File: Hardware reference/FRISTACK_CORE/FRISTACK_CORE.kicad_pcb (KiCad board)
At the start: 2 copper layers, 51 x 51 mm, 78 parts, among them J1 USB_C_Receptacle_USB2.0_16P, J2 JTAG_PIN_HEADER, J4 Conn_01x13_Socket, J5 Conn_01x13_Socket, J6 Conn_01x02_Pin, J7 Conn_01x02_Pin, U1 TPS62840DLCR, U2 USBLC6-2SC6, U3 ESP32-S3-MINI-1U, U4 FSUSB42MUX, U5 SN65HVD232, Y1 32.768 kHz

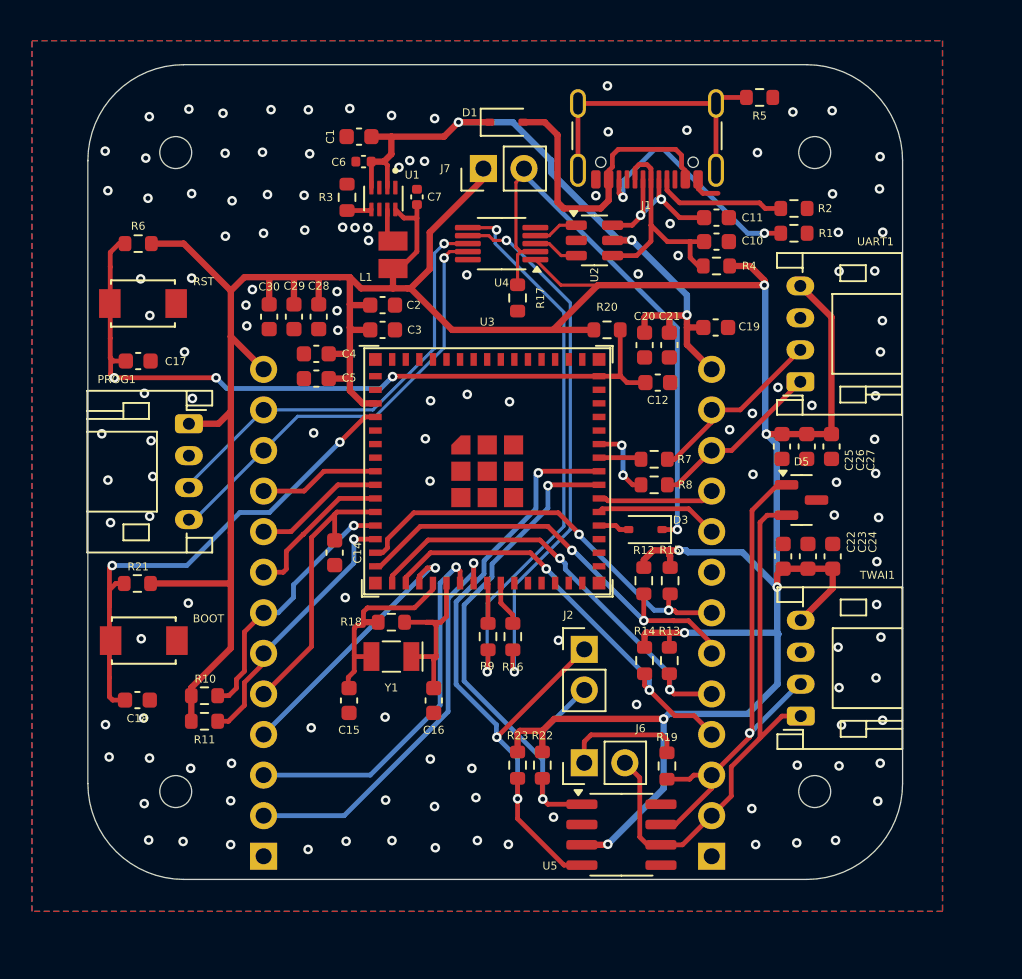
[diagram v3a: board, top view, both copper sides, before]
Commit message: Reworked CORE and adjusted header pins
Added USB switch and MCP73871 for charging battery and powering the system. Changed GPIO14 to BAT, dedicated for battery.
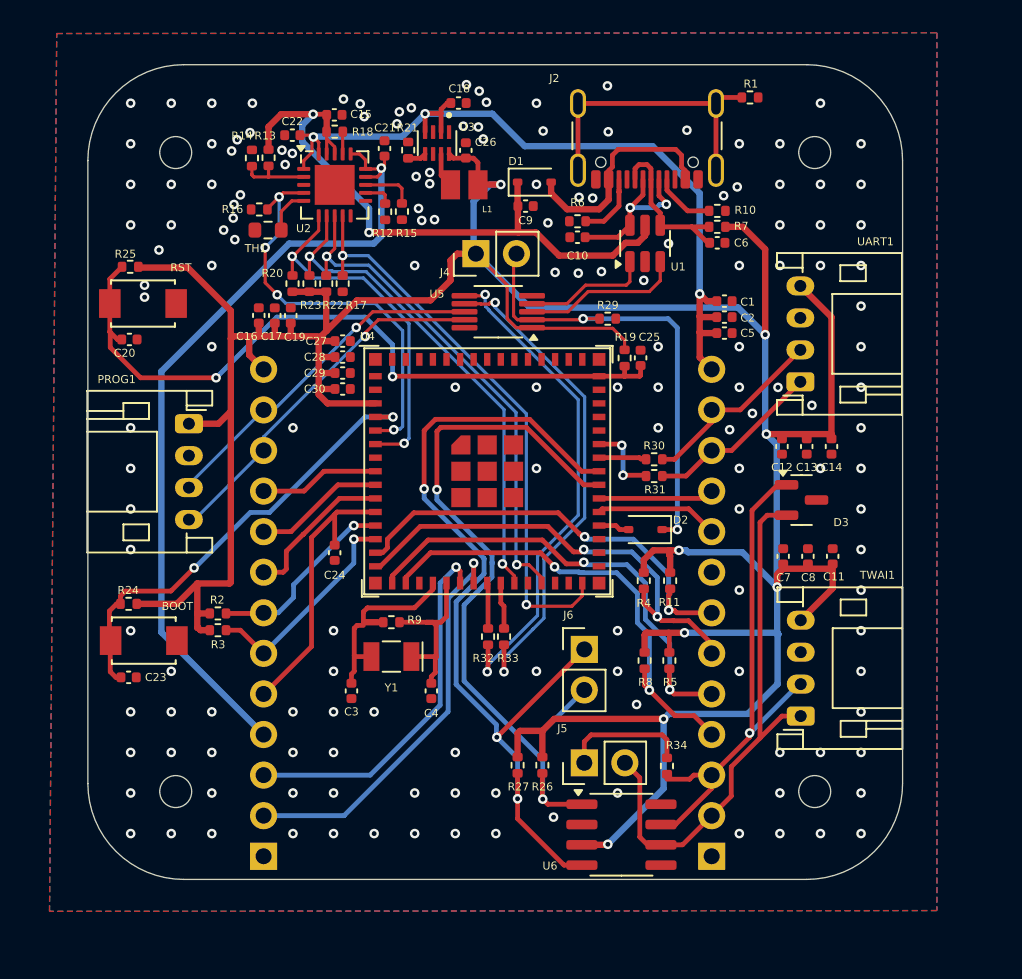
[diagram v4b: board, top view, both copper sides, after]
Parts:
- removed the C1 at (144.0, 76.5)
- removed the C11 at (166.3, 81.6)
- removed the C7 at (147.6, 80.3)
- removed J7: Conn_01x02_Pin, Connector_PinHeader_2.54mm:PinHeader_1x02_P2.54mm_Vertical
- removed the R1 at (171.2, 82.5)
- removed the R2 at (171.2, 81.0)
- removed the R3 at (143.2, 80.3)
- removed the R4 at (166.3, 84.6)
- removed the U4 at (152.9, 83.2)
- added C15: 10uf, Capacitor_SMD:C_0402_1005Metric, F.Cu at (142.4, 75.1)
- added C18: 4.7uF, Capacitor_SMD:C_0402_1005Metric, F.Cu at (150.2, 74.4)
- added C21: 4.7uF, Capacitor_SMD:C_0402_1005Metric, F.Cu at (145.6, 77.2)
- added C22: 4.7uF, Capacitor_SMD:C_0402_1005Metric, F.Cu at (139.8, 76.4)
- added C26: 10uF, Capacitor_SMD:C_0402_1005Metric, F.Cu at (150.7, 77.4)
- added C9: 10uf, Capacitor_SMD:C_0402_1005Metric, F.Cu at (154.4, 80.8)
- added J4: Conn_01x02_Pin, Connector_PinHeader_2.54mm:PinHeader_1x02_P2.54mm_Vertical, F.Cu at (151.3, 83.8)
- added R10: 5.1K, Resistor_SMD:R_0402_1005Metric, F.Cu at (166.4, 81.2)
- added R12: 20k, Resistor_SMD:R_0402_1005Metric, F.Cu at (145.6, 81.2)
- added R13: 330k, Resistor_SMD:R_0402_1005Metric, F.Cu at (138.3, 77.8)
- added R14: 110k, Resistor_SMD:R_0402_1005Metric, F.Cu at (137.3, 77.8)
- added R15: 2k, Resistor_SMD:R_0402_1005Metric, F.Cu at (146.7, 81.2)
- added R16: 10k, Resistor_SMD:R_0402_1005Metric, F.Cu at (137.7, 81.1)
- added R18: 10k, Resistor_SMD:R_0402_1005Metric, F.Cu at (142.4, 76.2)
- added R20: 10k, Resistor_SMD:R_0402_1005Metric, F.Cu at (139.8, 85.7)
- added R21: 267k, Resistor_SMD:R_0402_1005Metric, F.Cu at (147.1, 77.3)
- added R22: 10k, Resistor_SMD:R_0402_1005Metric, F.Cu at (141.9, 85.7)
- added R23: 10k, Resistor_SMD:R_0402_1005Metric, F.Cu at (140.9, 85.7)
- added R29: 10K, Resistor_SMD:R_0402_1005Metric, F.Cu at (159.5, 87.9)
- added R6: 5.1K, Resistor_SMD:R_0402_1005Metric, F.Cu at (157.7, 81.8)
- added R7: 10K, Resistor_SMD:R_0402_1005Metric, F.Cu at (166.4, 82.2)
- added TH1: 10k, Resistor_SMD:R_0603_1608Metric, F.Cu at (138.3, 82.4)
- added U1: USBLC6-2SC6, Package_TO_SOT_SMD:SOT-23-6, F.Cu at (161.9, 83.2)
- added U5: FSUSB42MUX, Package_SO:MSOP-10_3x3mm_P0.5mm, F.Cu at (152.7, 87.5)
- C1: renamed from C19; footprint Capacitor_SMD:C_0603_1608Metric -> Capacitor_SMD:C_0402_1005Metric
- C10: footprint Capacitor_SMD:C_0603_1608Metric -> Capacitor_SMD:C_0402_1005Metric
- C11: renamed from C24; footprint Capacitor_SMD:C_0603_1608Metric -> Capacitor_SMD:C_0402_1005Metric
- C12: renamed from C25; footprint Capacitor_SMD:C_0603_1608Metric -> Capacitor_SMD:C_0402_1005Metric
- C13: renamed from C26; footprint Capacitor_SMD:C_0603_1608Metric -> Capacitor_SMD:C_0402_1005Metric
- C14: renamed from C27; footprint Capacitor_SMD:C_0603_1608Metric -> Capacitor_SMD:C_0402_1005Metric
- C16: renamed from C28; footprint Capacitor_SMD:C_0603_1608Metric -> Capacitor_SMD:C_0402_1005Metric
- C17: renamed from C29; footprint Capacitor_SMD:C_0603_1608Metric -> Capacitor_SMD:C_0402_1005Metric
- C19: renamed from C30; footprint Capacitor_SMD:C_0603_1608Metric -> Capacitor_SMD:C_0402_1005Metric
- C2: renamed from C20; footprint Capacitor_SMD:C_0603_1608Metric -> Capacitor_SMD:C_0402_1005Metric
- C20: renamed from C17; footprint Capacitor_SMD:C_0603_1608Metric -> Capacitor_SMD:C_0402_1005Metric
- C23: renamed from C18; footprint Capacitor_SMD:C_0603_1608Metric -> Capacitor_SMD:C_0402_1005Metric
- C24: renamed from C14; footprint Capacitor_SMD:C_0603_1608Metric -> Capacitor_SMD:C_0402_1005Metric
- C25: renamed from C12; footprint Capacitor_SMD:C_0603_1608Metric -> Capacitor_SMD:C_0402_1005Metric
- C27: renamed from C2; footprint Capacitor_SMD:C_0603_1608Metric -> Capacitor_SMD:C_0402_1005Metric
- C28: renamed from C3; footprint Capacitor_SMD:C_0603_1608Metric -> Capacitor_SMD:C_0402_1005Metric
- C29: renamed from C4; footprint Capacitor_SMD:C_0603_1608Metric -> Capacitor_SMD:C_0402_1005Metric
- C3: renamed from C15; footprint Capacitor_SMD:C_0603_1608Metric -> Capacitor_SMD:C_0402_1005Metric
- C30: renamed from C5; footprint Capacitor_SMD:C_0603_1608Metric -> Capacitor_SMD:C_0402_1005Metric
- C4: renamed from C16; footprint Capacitor_SMD:C_0603_1608Metric -> Capacitor_SMD:C_0402_1005Metric
- C5: renamed from C21; footprint Capacitor_SMD:C_0603_1608Metric -> Capacitor_SMD:C_0402_1005Metric
- C6: value 4.7uF -> 10uf
- C7: renamed from C22; footprint Capacitor_SMD:C_0603_1608Metric -> Capacitor_SMD:C_0402_1005Metric
- C8: renamed from C23; footprint Capacitor_SMD:C_0603_1608Metric -> Capacitor_SMD:C_0402_1005Metric
- L1: footprint User imports:INDC2016X120N -> User_imports:INDC2016X120N
- R1: renamed from R5; footprint Resistor_SMD:R_0603_1608Metric -> Resistor_SMD:R_0402_1005Metric
- R11: renamed from R15; footprint Resistor_SMD:R_0603_1608Metric -> Resistor_SMD:R_0402_1005Metric
- R17: value 10K -> 10k; footprint Resistor_SMD:R_0603_1608Metric -> Resistor_SMD:R_0402_1005Metric
- R19: renamed from R20; footprint Resistor_SMD:R_0603_1608Metric -> Resistor_SMD:R_0402_1005Metric
- R2: renamed from R10; footprint Resistor_SMD:R_0603_1608Metric -> Resistor_SMD:R_0402_1005Metric
- R24: renamed from R21; footprint Resistor_SMD:R_0603_1608Metric -> Resistor_SMD:R_0402_1005Metric
- R25: renamed from R6; footprint Resistor_SMD:R_0603_1608Metric -> Resistor_SMD:R_0402_1005Metric
- R26: renamed from R22; footprint Resistor_SMD:R_0603_1608Metric -> Resistor_SMD:R_0402_1005Metric
- R27: renamed from R23; footprint Resistor_SMD:R_0603_1608Metric -> Resistor_SMD:R_0402_1005Metric
- R3: renamed from R11; footprint Resistor_SMD:R_0603_1608Metric -> Resistor_SMD:R_0402_1005Metric
- R30: renamed from R7; footprint Resistor_SMD:R_0603_1608Metric -> Resistor_SMD:R_0402_1005Metric
- R31: renamed from R8; footprint Resistor_SMD:R_0603_1608Metric -> Resistor_SMD:R_0402_1005Metric
- R32: renamed from R9; footprint Resistor_SMD:R_0603_1608Metric -> Resistor_SMD:R_0402_1005Metric
- R33: renamed from R16; footprint Resistor_SMD:R_0603_1608Metric -> Resistor_SMD:R_0402_1005Metric
- R34: renamed from R19; footprint Resistor_SMD:R_0603_1608Metric -> Resistor_SMD:R_0402_1005Metric
- R4: renamed from R12; footprint Resistor_SMD:R_0603_1608Metric -> Resistor_SMD:R_0402_1005Metric
- R5: renamed from R13; footprint Resistor_SMD:R_0603_1608Metric -> Resistor_SMD:R_0402_1005Metric
- R8: renamed from R14; footprint Resistor_SMD:R_0603_1608Metric -> Resistor_SMD:R_0402_1005Metric
- R9: renamed from R18; footprint Resistor_SMD:R_0603_1608Metric -> Resistor_SMD:R_0402_1005Metric
- U2: value USBLC6-2SC6 -> MCP73871-2CC; footprint Package_TO_SOT_SMD:SOT-23-6 -> Package_DFN_QFN:QFN-20-1EP_4x4mm_P0.5mm_EP2.5x2.5mm
- moved C6 22.7 mm to (166.4, 83.2), turned to 0 degrees
- moved U2 16.6 mm to (142.4, 79.5)
- moved R17 11.0 mm to (142.9, 85.7)
- moved C10 8.70 mm to (157.7, 82.8), turned to 180 degrees
- moved G*** 7.01 mm to (151.9, 76.8)
- moved L1 6.25 mm to (150.6, 79.5), turned to 0 degrees
- moved R3 5.76 mm to (135.1, 107.4)
- moved C2 5.30 mm to (166.8, 87.8), turned to 0 degrees
- moved R2 5.22 mm to (135.1, 106.3)
- moved U3 4.83 mm to (148.9, 76.9)
- moved D1 4.14 mm to (154.9, 79.3)
- moved C16 3.75 mm to (137.7, 87.7), turned to 90 degrees
- moved C5 3.53 mm to (166.8, 88.8), turned to 0 degrees
- moved C27 3.36 mm to (142.9, 89.3)
- moved C28 3.02 mm to (142.9, 90.3)
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- renumbered D3 to D2, D5 to D3, J4 to J1, J1 to J2, J5 to J3, J6 to J5, J2 to J6, U1 to U3, U3 to U4, U5 to U6
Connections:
- C1 pad 1: +5V -> OUT/BAT
- C10 pad 1: USB_P -> USB_N
- C2 pad 1: +5V -> OUT/BAT
- C5 pad 1: +5V -> OUT/BAT
- C6 pad 1: +5V -> USB_P
- D1 pad 1: +5V -> VBUS
- J1 pad 4: GPIO14 -> BAT
- J3 pad 13: +5V -> OUT/BAT
- R17 pad 1: SEL -> GPIO48
- U2 pad 1: USB_N_2 -> OUT/BAT
- U2 pad 2: GND -> Net-(U2-VPCC)
- U2 pad 3: USB_P_2 -> GND
- U2 pad 4: USB_P -> GPIO1
- U2 pad 5: +5V -> Net-(U2-THERM)
- U2 pad 6: USB_N -> PG
- U3 pad 2: +5V -> OUT/BAT
- U3 pad 4: +5V -> OUT/BAT
- U4 pad 18: GPIO14 -> unconnected-(U4-IO14-Pad18)
- U4 pad 25: unconnected-(U3-IO21-Pad25) -> STAT2
- U4 pad 27: unconnected-(U3-IO47-Pad27) -> STAT1
- U4 pad 30: unconnected-(U3-IO48-Pad30) -> GPIO48
- U4 pad 5: unconnected-(U3-IO1-Pad5) -> GPIO1
- U4 pad 6: unconnected-(U3-IO2-Pad6) -> PG
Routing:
- net BAT: track 0.00 -> 51.7 mm, vias 0 -> 1
- net OUT/BAT: track 0.00 -> 50.4 mm, vias 0 -> 3
- net +5V: track 45.2 -> 0.00 mm, vias 3 -> 0
- net VBUS: track 0.00 -> 40.6 mm, vias 0 -> 2
- net GPIO48: track 0.00 -> 35.9 mm, vias 0 -> 2
- net STAT1: track 0.00 -> 31.6 mm, vias 0 -> 2
- net STAT2: track 0.00 -> 31.6 mm, vias 0 -> 2
- net GPIO1: track 0.00 -> 26.2 mm, vias 0 -> 4
- net PG: track 0.00 -> 23.0 mm, vias 0 -> 2
- net GPIO14: track 16.7 -> 0.00 mm, vias 1 -> 0
- net CAN_D: track 36.4 -> 48.3 mm
- net CAN_R: track 43.5 -> 55.0 mm
- net Net-(J2-CC2): track 15.2 -> 4.32 mm, vias 2 -> 0
- net USB_P_2: track 2.87 -> 10.0 mm
- net SEL: track 36.3 -> 29.3 mm, vias 1 -> 2
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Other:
- board text added: "TWAI TERMINATION"
- board text added: "USB SELECT"

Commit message: Changed jumpers with DIP switches and adjusted copper areas
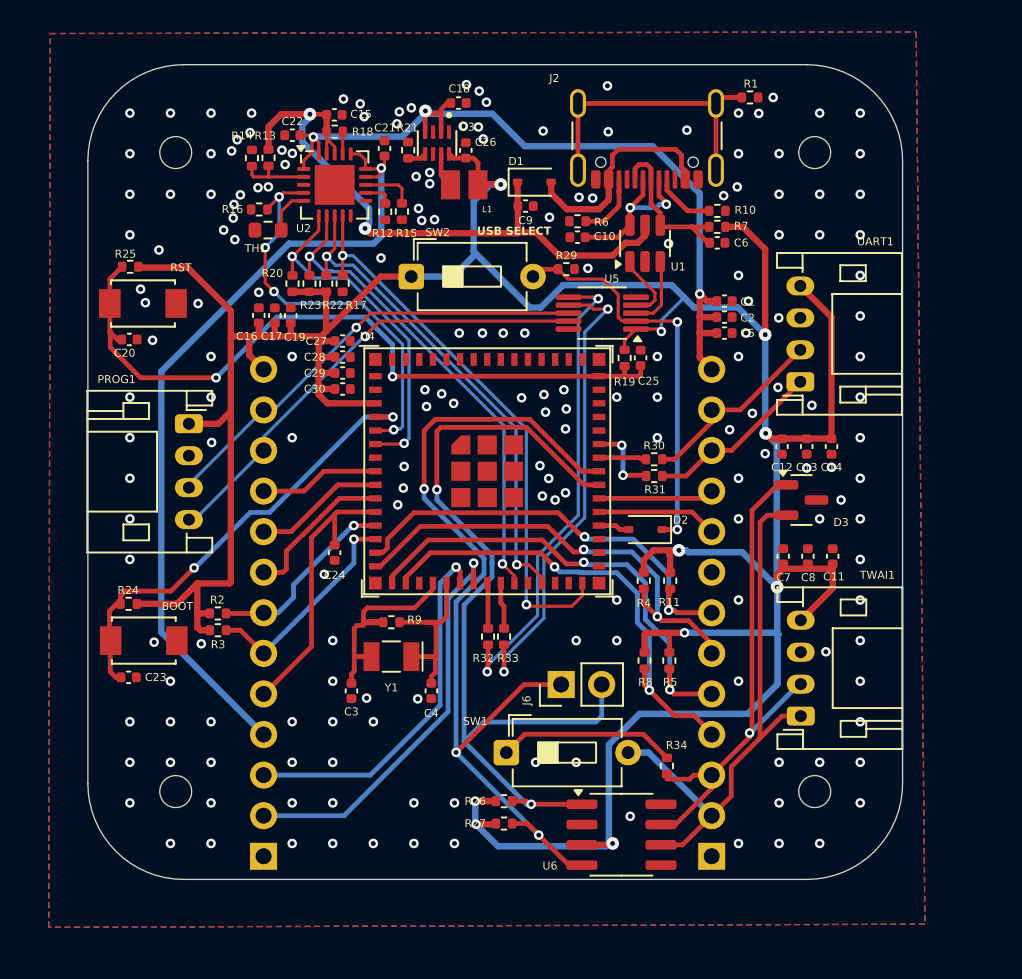
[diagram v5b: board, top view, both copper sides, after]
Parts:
- removed J4, J5: Conn_01x02_Pin, Connector_PinHeader_2.54mm:PinHeader_1x02_P2.54mm_Vertical
- added SW1: SW_DIP_x01, Button_Switch_THT:SW_DIP_SPSTx01_Slide_6.7x4.1mm_W7.62mm_P2.54mm_LowProfile, F.Cu at (153.2, 115.1)
- added SW2: SW_DIP_x01, Button_Switch_THT:SW_DIP_SPSTx01_Slide_6.7x4.1mm_W7.62mm_P2.54mm_LowProfile, F.Cu at (147.2, 85.3)
- moved U5 6.51 mm to (159.2, 87.5)
- moved R29 4.04 mm to (156.9, 84.8)
- moved R27 3.75 mm to (153.1, 119.5), turned to 0 degrees
- moved R26 3.29 mm to (153.1, 118.1), turned to 180 degrees
- moved J6 2.63 mm to (156.6, 110.8), turned to 90 degrees
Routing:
- net USB_P_HD: track 23.1 -> 29.7 mm
- net CAN_D: track 48.3 -> 54.9 mm
- net USB_N_HD: track 22.2 -> 28.7 mm
- net USB_P_2: track 10.0 -> 4.55 mm
- net ESP_PWR: track 226.6 -> 222.6 mm, vias 8 -> 10
- net SEL: track 29.3 -> 25.4 mm
- net USB_N_2: track 7.95 -> 4.37 mm
- net Net-(R34-Pad2): track 7.63 -> 11.1 mm
- net USB_N_ESP: track 31.1 -> 29.5 mm
- net USB_P_ESP: track 31.2 -> 29.6 mm
- net CAN_R: track 55.0 -> 56.1 mm
- net CAN_L: track 35.1 -> 35.8 mm
- net PG: track 23.0 -> 22.3 mm
- net STAT2: track 31.6 -> 31.0 mm
- net STAT1: track 31.6 -> 31.1 mm
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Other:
- board text added: "BAT"
- board text removed: "GPIO14"

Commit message: changed mouting holes
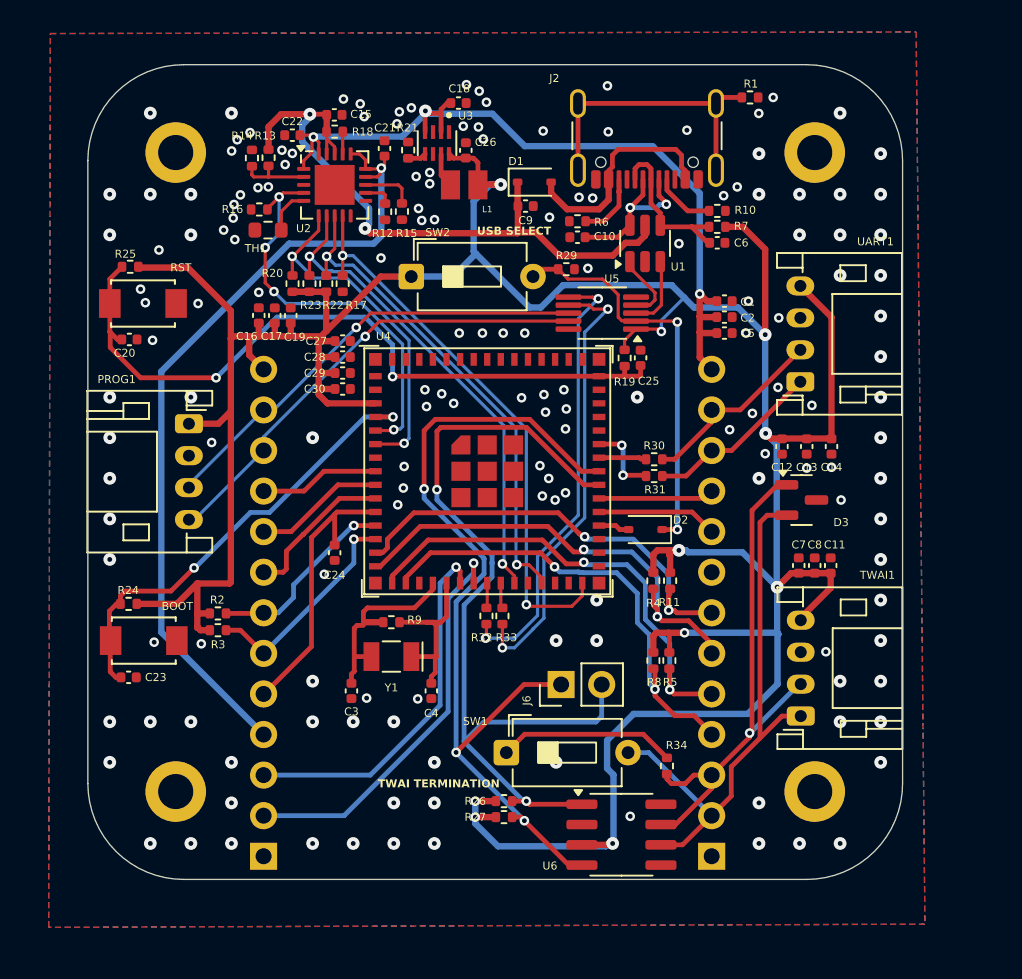
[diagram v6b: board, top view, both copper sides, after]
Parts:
- removed the REF** at (132.5, 117.5)
- removed the REF** at (172.5, 117.5)
- removed the REF** at (132.5, 77.5)
- removed the REF** at (172.5, 77.5)
- added REF**: MountingHole_2.2mm_M2_DIN965_Pad, MountingHole:MountingHole_2.2mm_M2_DIN965_Pad, F.Cu at (132.5, 77.5)
- added REF**: MountingHole_2.2mm_M2_DIN965_Pad, MountingHole:MountingHole_2.2mm_M2_DIN965_Pad, F.Cu at (172.5, 117.5)
- added REF**: MountingHole_2.2mm_M2_DIN965_Pad, MountingHole:MountingHole_2.2mm_M2_DIN965_Pad, F.Cu at (172.5, 77.5)
- added REF**: MountingHole_2.2mm_M2_DIN965_Pad, MountingHole:MountingHole_2.2mm_M2_DIN965_Pad, F.Cu at (132.5, 117.5)
- moved R32 1.29 mm to (151.9, 106.5)
- moved R33 1.29 mm to (152.9, 106.5)
- moved C7 1.13 mm to (171.5, 103.3)
- moved C8 0.72 mm to (172.5, 103.3)
- moved R4 0.60 mm to (162.4, 104.3)
- moved C11 0.59 mm to (173.5, 103.3)
- moved R8 0.55 mm to (162.4, 109.3)
- moved R27 0.40 mm to (153.1, 119.1)
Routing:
- net ESP_PWR: track 222.6 -> 221.1 mm
- net USB_N_ESP: track 29.5 -> 28.0 mm
- net Net-(U4-USB_D+): track 2.92 -> 1.59 mm
- net USB_P_ESP: track 29.6 -> 28.4 mm
- net CAN_R: track 56.1 -> 55.0 mm
- net Net-(U4-USB_D-): track 2.55 -> 1.57 mm
- net CAN_H: track 35.4 -> 35.9 mm
- net GND: vias 186 -> 162

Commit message: review and new BATTERY board
IOT - changed twai termination from header to switch option, new holes , added power planes
SENSOR NODE - new holes and back silk text
CORE - vertical twai termination header changed to horizontal
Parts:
- J6: footprint Connector_PinHeader_2.54mm:PinHeader_1x02_P2.54mm_Vertical -> Connector_PinHeader_2.54mm:PinHeader_1x02_P2.54mm_Horizontal
- moved J6 9.16 mm to (147.6, 112.1), turned to -90 degrees
- moved C4 1.89 mm to (149.8, 109.8), turned to 180 degrees
- moved C3 1.72 mm to (142.5, 109.8), turned to 0 degrees
- moved G*** 0.74 mm to (151.7, 77.5)
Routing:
- net CAN_R: track 55.0 -> 49.2 mm
- net CAN_D: track 54.5 -> 49.7 mm, vias 2 -> 3
- net X_TAL_N: track 10.9 -> 9.96 mm
- net GPIO17: track 23.0 -> 23.7 mm
- net GPIO18: track 25.5 -> 26.1 mm
- net X_TAL_P: track 12.2 -> 11.6 mm
- net GND: vias 162 -> 165
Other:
- board text added: "Designed by Andrej Šimkovič & Marián Bobček 2025"
